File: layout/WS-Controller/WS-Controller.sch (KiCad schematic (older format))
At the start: 41 parts, among them J2 Conn_01x06, J4 Conn_01x06, J6 Conn_01x15, J7 Conn_01x15, J8 Conn_01x04, J9 Conn_01x04, K1 G5V-2, K2 G5V-2, M2 Jumper, Q1 BC547, Q2 BC547

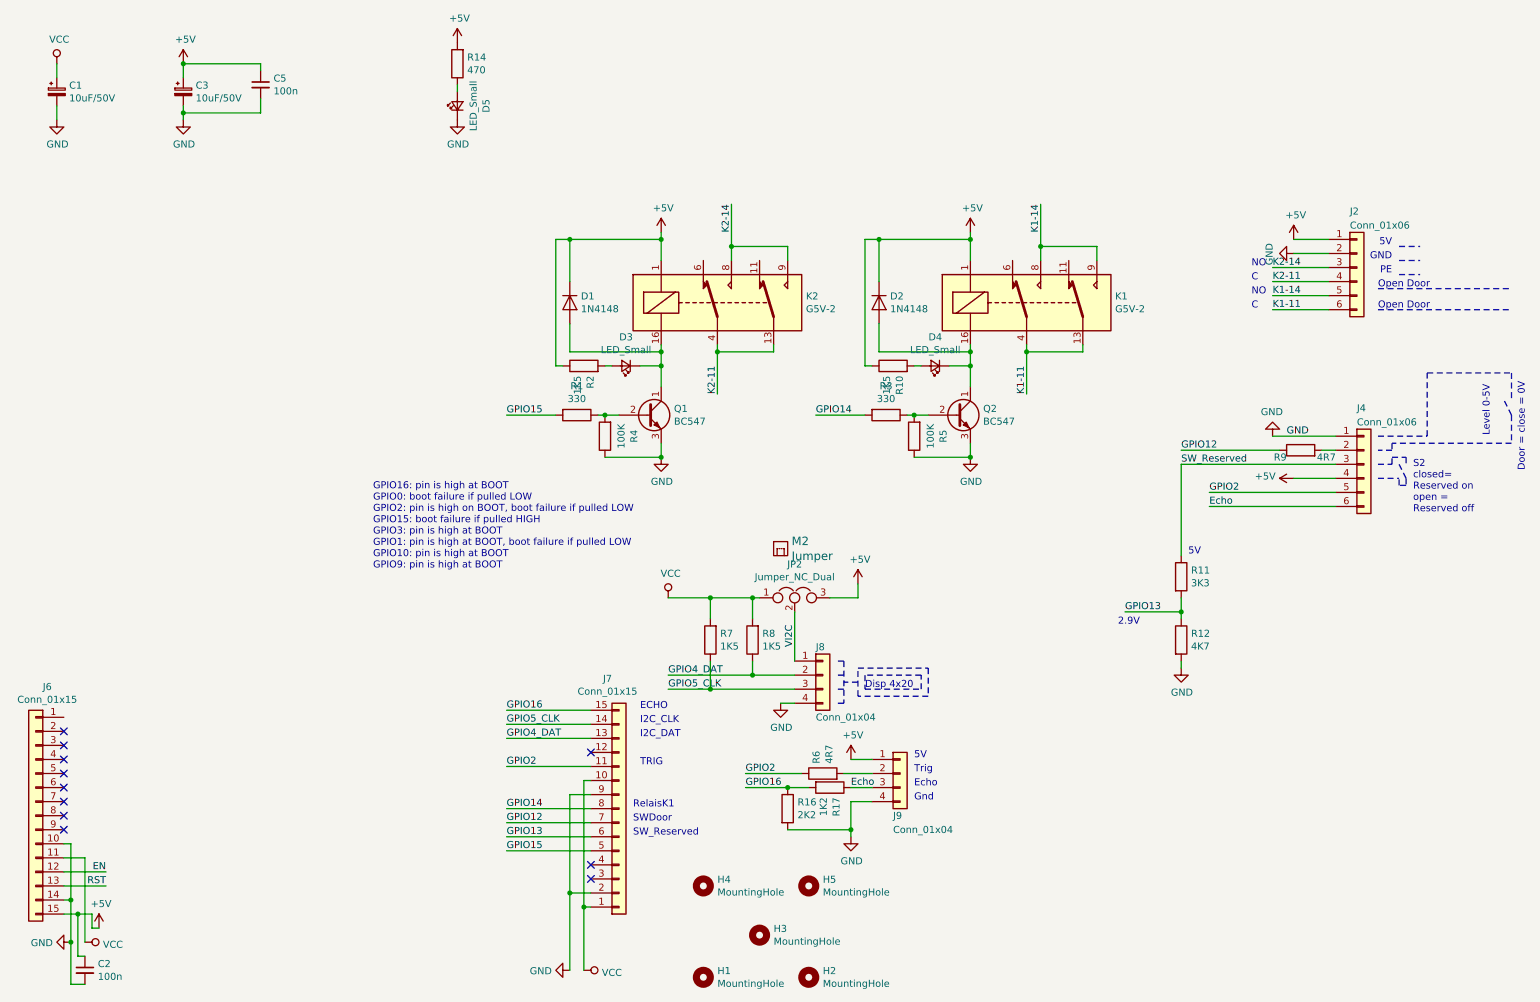
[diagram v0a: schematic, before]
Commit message: Schaltplan für Wemos-D1
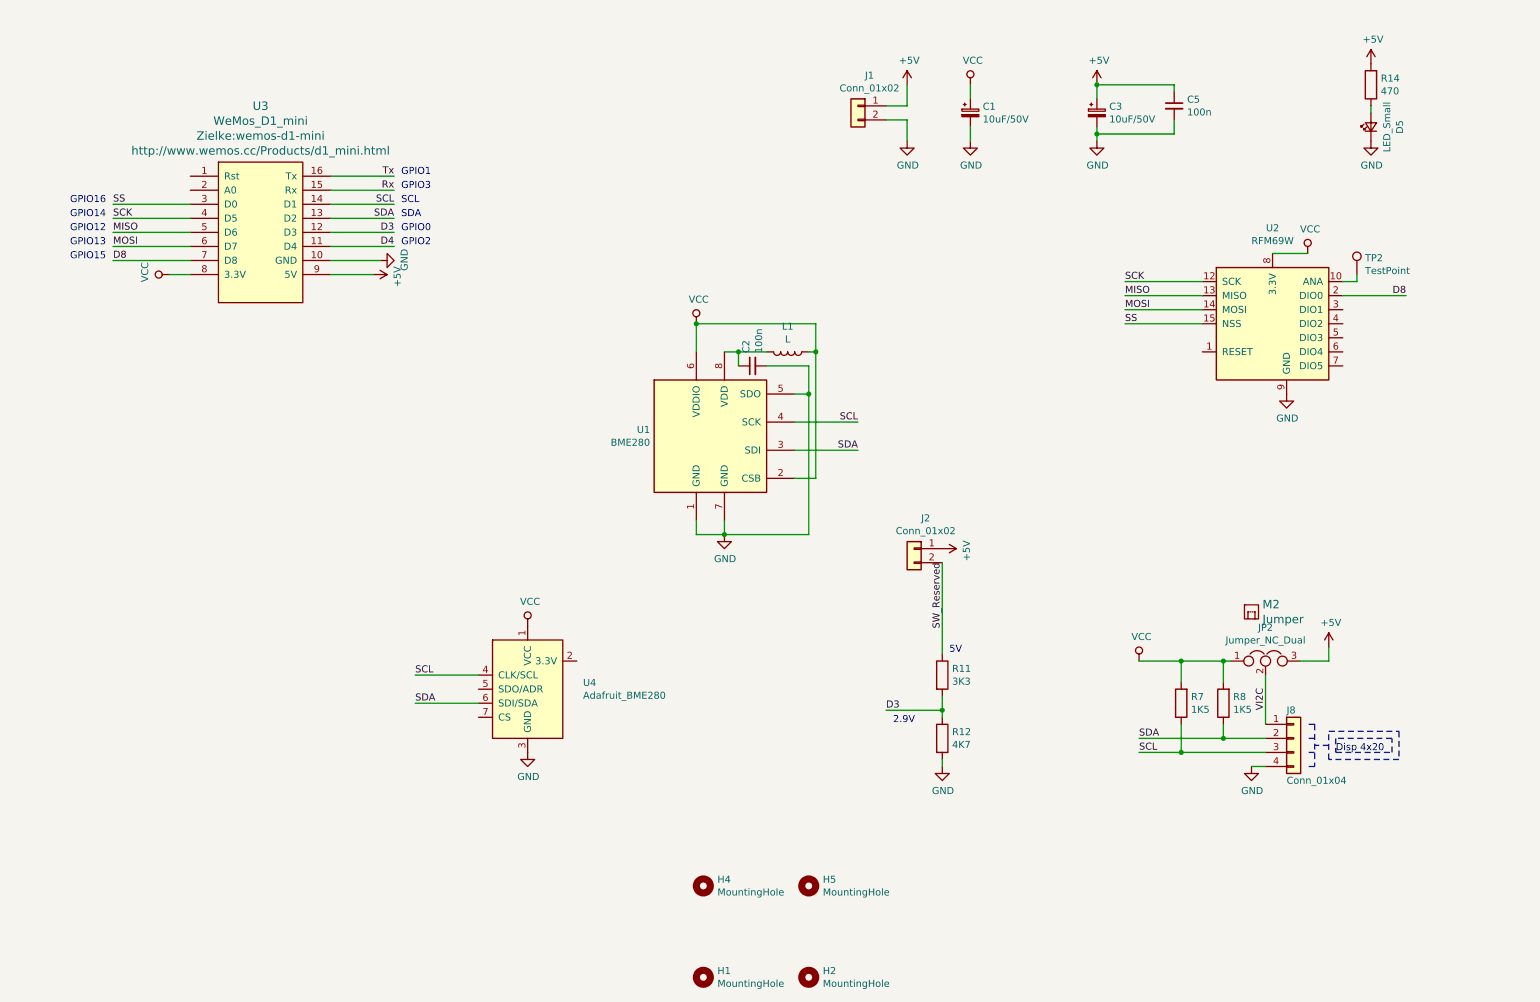
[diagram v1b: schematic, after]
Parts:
- removed D1, D2: 1N4148, Diode_THT:D_DO-35_SOD27_P7.62mm_Horizontal, symbol Diode:1N4148
- removed D3, D4: LED_Small, LED_THT:LED_D3.0mm, symbol Device:LED_Small
- removed H3: MountingHole, MountingHole:MountingHole_4.3mm_M4_ISO14580, symbol Mechanical:MountingHole
- removed J2, J4: Conn_01x06, Connector_Phoenix_MSTB:PhoenixContact_MSTBA_2,5_6-G-5,08_1x06_P5.08mm_Horizontal, symbol Connector_Generic:Conn_01x06
- removed J6, J7: Conn_01x15, Connector_PinSocket_2.54mm:PinSocket_1x15_P2.54mm_Vertical, symbol Connector_Generic:Conn_01x15
- removed J9: Conn_01x04, kp_Connectors_Wuerth:WR-WTB-04-V, symbol Connector_Generic:Conn_01x04
- removed K1, K2: G5V-2, Relay_THT:Relay_DPDT_Omron_G5V-2, symbol Relay:G5V-2
- removed Q1, Q2: BC547, Package_TO_SOT_THT:TO-92_Inline, symbol Transistor_BJT:BC547
- removed R1, R3: 330, Resistor_SMD:R_0603_1608Metric, symbol Device:R
- removed R10, R2: 1K5, Resistor_SMD:R_0603_1608Metric, symbol Device:R
- removed R16: 2K2, Resistor_SMD:R_0603_1608Metric, symbol Device:R
- removed R17: 1K2, Resistor_SMD:R_0603_1608Metric, symbol Device:R
- removed R4, R5: 100K, Resistor_SMD:R_0603_1608Metric, symbol Device:R
- removed R6, R9: 4R7, Resistor_SMD:R_0603_1608Metric, symbol Device:R
- added J1, J2: Conn_01x02, TerminalBlock_Phoenix:TerminalBlock_Phoenix_MKDS-1,5-2-5.08_1x02_P5.08mm_Horizontal, symbol Connector_Generic:Conn_01x02
- added L1: L, Inductor_SMD:L_2010_5025Metric, symbol Device:L
- added TP2: TestPoint, TestPoint:TestPoint_THTPad_2.0x2.0mm_Drill1.0mm, symbol Connector:TestPoint
- added U1: BME280, Package_LGA:Bosch_LGA-8_2.5x2.5mm_P0.65mm_ClockwisePinNumbering, symbol Sensor:BME280
- added U2: RFM69W, RF_Module:HOPERF_RFM69HW, symbol RF_AM_FM:RFM69W
- added U3: WeMos_D1_mini, Zielke:wemos-d1-mini, symbol wemos_mini:WeMos_D1_mini
- added U4: Adafruit_BME280, Zielke:ADAFRUIT_BME280, symbol BreakoutBoards:Adafruit_BME280
- J8: footprint kp_Connectors_Wuerth:WR-WTB-04-V -> Connector_Molex:Molex_KK-254_AE-6410-04A_1x04_P2.54mm_Vertical
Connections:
- net +5V: now also J1.1 (Pin_1), J2.1 (Pin_1), U3.9 (5V); no longer C2.1
- net GND: now also J1.2 (Pin_2), U1.1 (GND), U1.5 (SDO), U1.7 (GND), U2.11 (GND), U2.9 (GND), U3.10 (GND), U4.3 (GND)
- net SW_Reserved: now also J2.2 (Pin_2)
- net VCC: now also L1.1, U1.2 (CSB), U1.6 (VDDIO), U2.8 (3.3V), U3.8 (3.3V), U4.1 (VCC)
- net GPIO13 renamed D3
- net D3: now also U3.12 (D3)
- net GPIO4_DAT renamed SDA
- net SDA: now also U1.3 (SDI), U3.13 (D2), U4.6 (SDI/SDA)
- net GPIO5_CLK renamed SCL
- net SCL: now also U1.4 (SCK), U3.14 (D1), U4.4 (CLK/SCL)
- new net: TP2.1, U2.10 (ANA)
- new net: C2.1, L1.2, U1.8 (VDD)
- new net D4: U3.11 (D4)
- new net D8: U2.2 (DIO0), U3.7 (D8)
- new net MISO: U2.13 (MISO), U3.5 (D6)
- new net MOSI: U2.14 (MOSI), U3.6 (D7)
- new net Rx: U3.15 (Rx)
- new net SCK: U2.12 (SCK), U3.4 (D5)
- new net SS: U2.15 (NSS), U3.3 (D0)
- new net Tx: U3.16 (Tx)
- no-connect marks 11 -> 0
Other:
- note added: "GPIO0"
- note added: "GPIO1"
- note added: "GPIO12"
- note added: "GPIO13"
- note added: "GPIO14"
- note added: "GPIO15"
- note added: "GPIO16"
- note added: "GPIO2"
- note added: "GPIO3"
- note added: "SCL"
- note added: "SDA"
- note removed: "C"
- note removed: "Door = close = 0V"
- note removed: "ECHO"
- note removed: "Echo"
- note removed: "GND"
- note removed: "GPIO16: pin is high at BOOT\nGPIO0: boot failure if pulled LOW\nGPIO2: pin is high on BOOT, boot failure if pulled LOW\nGPIO15: boot failure if pulled HIGH\nGPIO3: pin is high at BOOT\nGPIO1: pin is high at BOOT, boot failure if pulled LOW\nGPIO10: pin is high at BOOT\nGPIO9: pin is high at BOOT"
- note removed: "Gnd"
- note removed: "I2C_CLK"
- note removed: "I2C_DAT"
- note removed: "Level 0-5V"
- note removed: "NO"
- note removed: "Open Door"
- note removed: "PE"
- note removed: "RelaisK1"
- note removed: "S2\nclosed=\nReserved on\nopen =\nReserved off"
- note removed: "SWDoor"
- note removed: "SW_Reserved"
- note removed: "TRIG"
- note removed: "Trig"
- moved on the sheet: C1, C3, C5, D5, J8, JP2, M2, R11, R12, R14, R7, R8
